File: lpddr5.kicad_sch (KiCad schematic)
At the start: 38 parts, among them U1 MT62F1G32D4DR-031_WT:B

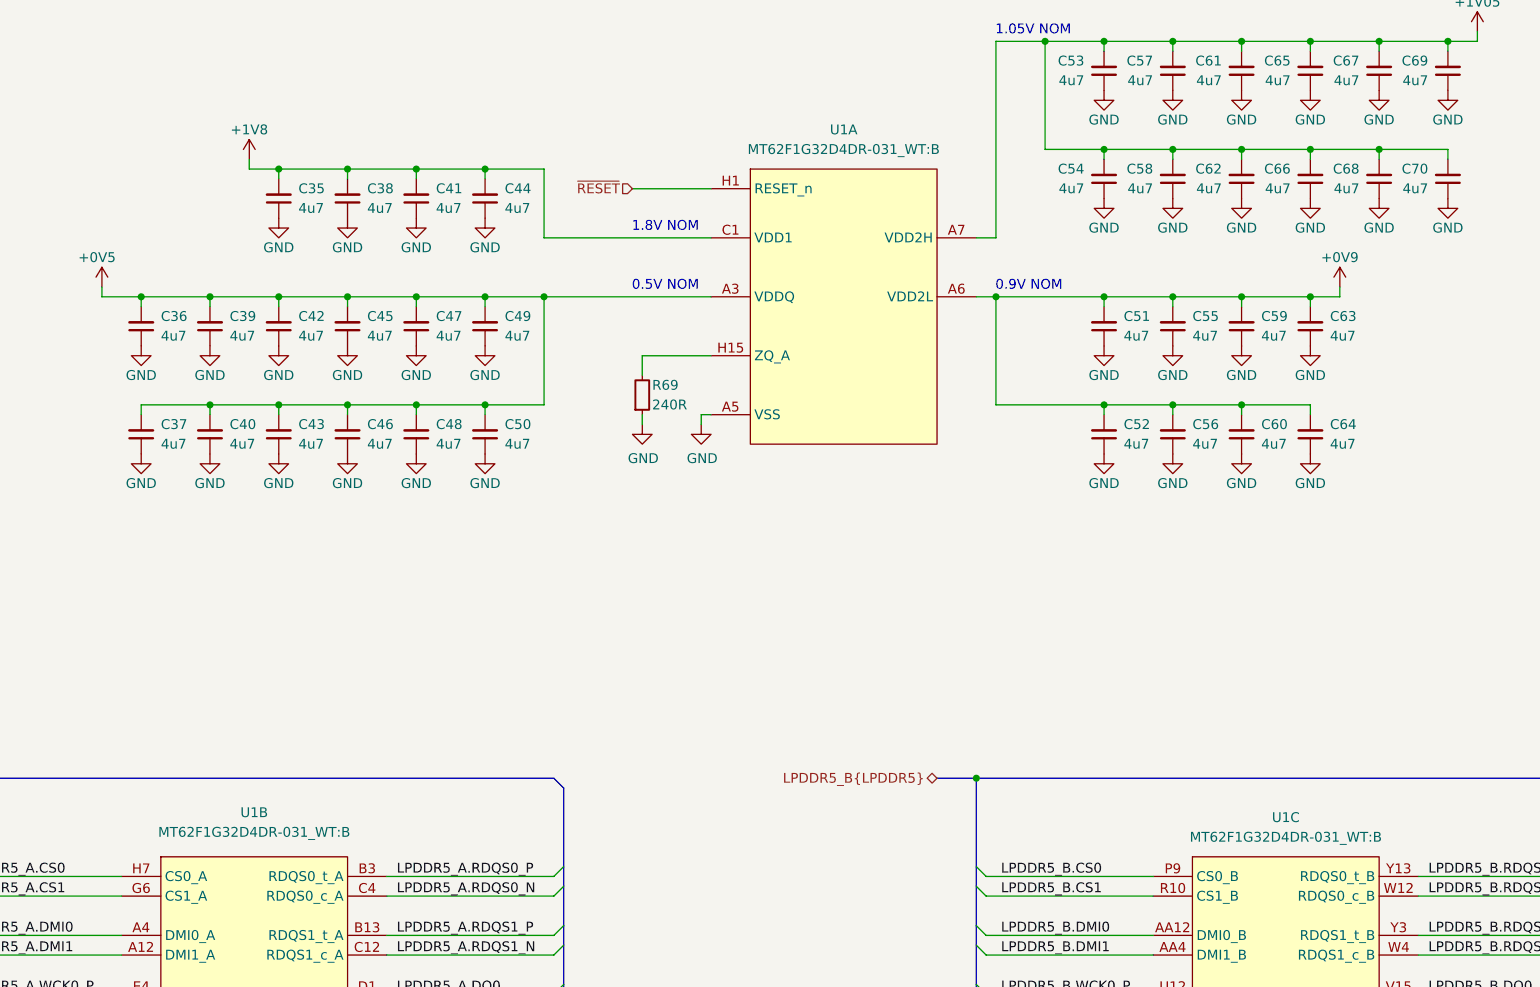
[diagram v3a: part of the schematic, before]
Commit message: [#52835] schematics: update components after standardization
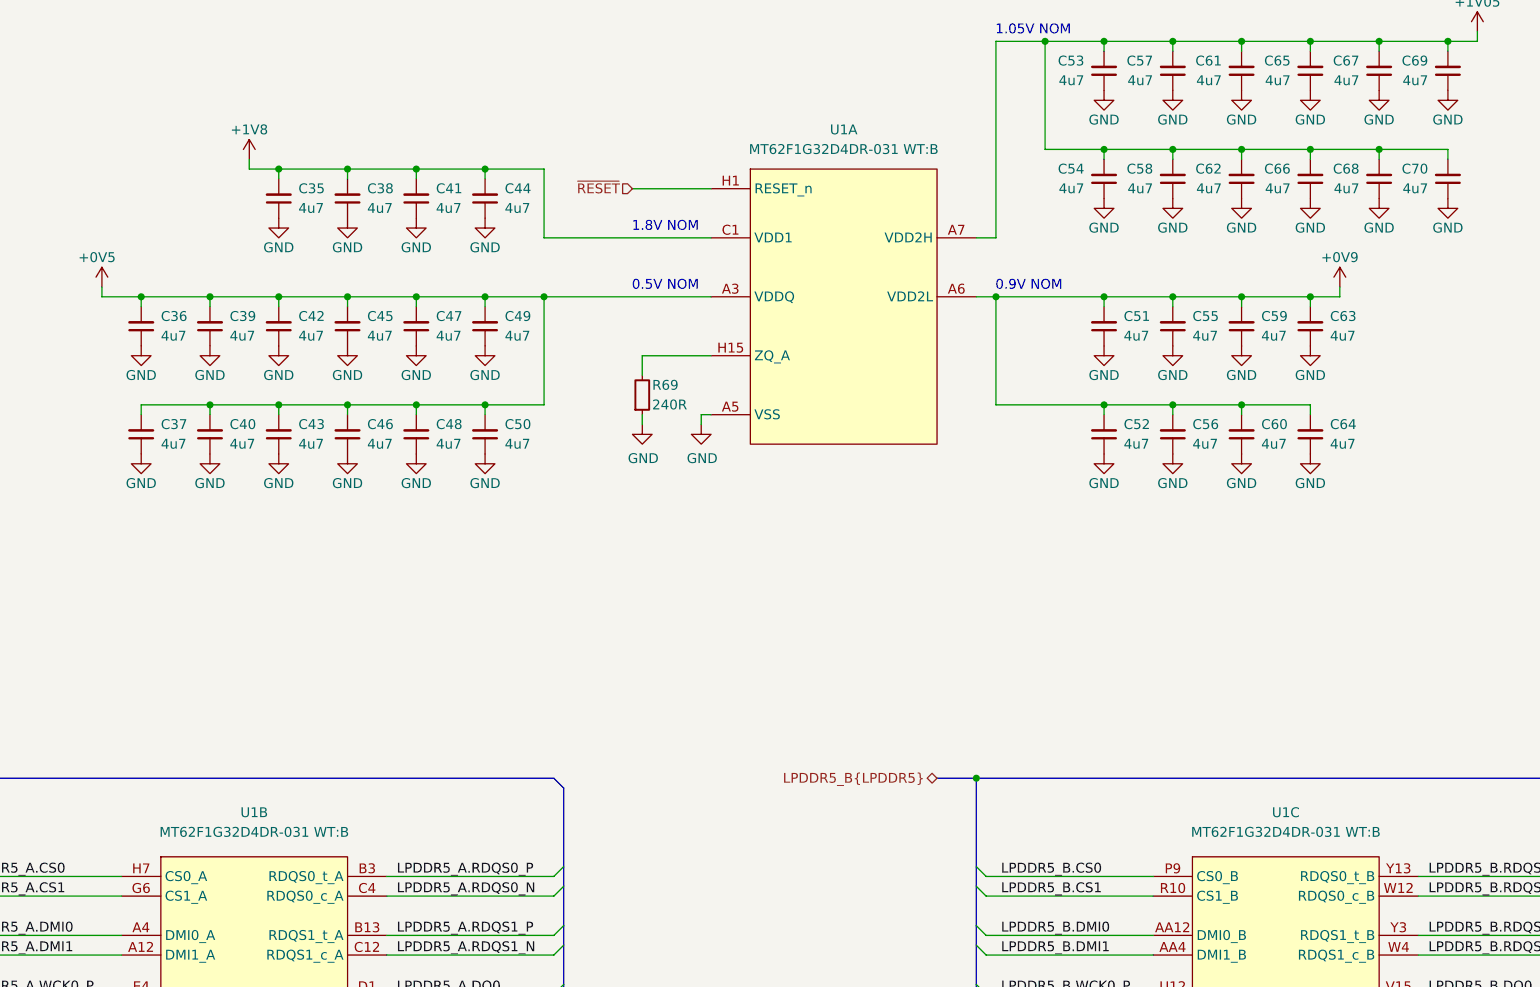
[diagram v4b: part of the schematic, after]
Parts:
- removed U1: MT62F1G32D4DR-031_WT:B, antmicro-footprints:BGA-315_12.4x15mm_Layout15x21_P0.7x0.8mm, symbol antmicroMemory:MT62F1G32D4DR-031_WT{colon}B
- added U1: MT62F1G32D4DR-031, antmicro-footprints:BGA-315_12.4x15mm_Layout15x21_P0.8x0.7mm, symbol antmicroMemory:MT62F1G32D4DR-031
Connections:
- net +0V5: now also U1.A13 (VDDQ), U1.A3 (VDDQ), U1.AA13 (VDDQ), U1.AA3 (VDDQ), U1.B14 (VDDQ), U1.B2 (VDDQ), U1.C13 (VDDQ), U1.C3 (VDDQ), U1.D12 (VDDQ), U1.D4 (VDDQ), U1.E11 (VDDQ), U1.E5 (VDDQ), U1.F1 (VDDQ), U1.F12 (VDDQ), U1.F13 (VDDQ), U1.F15 (VDDQ), U1.F3 (VDDQ), U1.F4 (VDDQ), U1.G1 (VDDQ), U1.G14 (VDDQ), U1.G15 (VDDQ), U1.G2 (VDDQ), U1.R1 (VDDQ), U1.R14 (VDDQ), U1.R15 (VDDQ), U1.R2 (VDDQ), U1.T1 (VDDQ), U1.T12 (VDDQ), U1.T13 (VDDQ), U1.T15 (VDDQ), U1.T3 (VDDQ), U1.T4 (VDDQ), U1.U11 (VDDQ), U1.U5 (VDDQ), U1.V12 (VDDQ), U1.V4 (VDDQ), U1.W13 (VDDQ), U1.W3 (VDDQ), U1.Y14 (VDDQ), U1.Y2 (VDDQ)
- net +0V9: now also U1.A10 (VDD2L), U1.A6 (VDD2L), U1.AA10 (VDD2L), U1.AA6 (VDD2L), U1.B10 (VDD2L), U1.B6 (VDD2L), U1.H14 (VDD2L), U1.H2 (VDD2L), U1.J14 (VDD2L), U1.J2 (VDD2L), U1.N14 (VDD2L), U1.N2 (VDD2L), U1.P14 (VDD2L), U1.P2 (VDD2L), U1.Y10 (VDD2L), U1.Y6 (VDD2L)
- net +1V05: now also U1.A7 (VDD2H), U1.A8 (VDD2H), U1.A9 (VDD2H), U1.AA7 (VDD2H), U1.AA8 (VDD2H), U1.AA9 (VDD2H), U1.B7 (VDD2H), U1.B9 (VDD2H), U1.C7 (VDD2H), U1.C9 (VDD2H), U1.D8 (VDD2H), U1.E7 (VDD2H), U1.E9 (VDD2H), U1.F10 (VDD2H), U1.F6 (VDD2H), U1.F7 (VDD2H), U1.F9 (VDD2H), U1.J11 (VDD2H), U1.J5 (VDD2H), U1.K1 (VDD2H), U1.K10 (VDD2H), U1.K11 (VDD2H), U1.K12 (VDD2H), U1.K13 (VDD2H), U1.K14 (VDD2H), U1.K15 (VDD2H), U1.K2 (VDD2H), U1.K3 (VDD2H), U1.K4 (VDD2H), U1.K5 (VDD2H), U1.K6 (VDD2H), U1.L10 (VDD2H), U1.L6 (VDD2H), U1.L7 (VDD2H), U1.L8 (VDD2H), U1.L9 (VDD2H), U1.M1 (VDD2H), U1.M10 (VDD2H), U1.M11 (VDD2H), U1.M12 (VDD2H), U1.M13 (VDD2H), U1.M14 (VDD2H), U1.M15 (VDD2H), U1.M2 (VDD2H), U1.M3 (VDD2H), U1.M4 (VDD2H), U1.M5 (VDD2H), U1.M6 (VDD2H), U1.N11 (VDD2H), U1.N5 (VDD2H), U1.T10 (VDD2H), U1.T6 (VDD2H), U1.T7 (VDD2H), U1.T9 (VDD2H), U1.U7 (VDD2H), U1.U9 (VDD2H), U1.V8 (VDD2H), U1.W7 (VDD2H), U1.W9 (VDD2H), U1.Y7 (VDD2H), U1.Y9 (VDD2H)
- net +1V8: now also U1.C1 (VDD1), U1.C15 (VDD1), U1.W1 (VDD1), U1.W15 (VDD1)
- net GND: now also U1.A11 (VSS), U1.A5 (VSS), U1.AA11 (VSS), U1.AA5 (VSS), U1.B12 (VSS), U1.B4 (VSS), U1.B8 (VSS), U1.C11 (VSS), U1.C5 (VSS), U1.C8 (VSS), U1.D10 (VSS), U1.D14 (VSS), U1.D2 (VSS), U1.D6 (VSS), U1.D7 (VSS), U1.D9 (VSS), U1.E1 (VSS), U1.E13 (VSS), U1.E15 (VSS), U1.E3 (VSS), U1.E8 (VSS), U1.F14 (VSS), U1.F2 (VSS), U1.F8 (VSS), U1.G11 (VSS), U1.G13 (VSS), U1.G3 (VSS), U1.G5 (VSS), U1.G7 (VSS), U1.G9 (VSS), U1.H10 (VSS), U1.H12 (VSS), U1.H3 (VSS), U1.H4 (VSS), U1.H6 (VSS), U1.H8 (VSS), U1.J1 (VSS), U1.J10 (VSS), U1.J12 (VSS), U1.J13 (VSS), U1.J15 (VSS), U1.J3 (VSS), U1.J7 (VSS), U1.J8 (VSS), U1.K7 (VSS), U1.K8 (VSS), U1.K9 (VSS), U1.L1 (VSS), U1.L11 (VSS), U1.L12 (VSS), U1.L13 (VSS), U1.L14 (VSS), U1.L15 (VSS), U1.L2 (VSS), U1.L3 (VSS), U1.L4 (VSS), U1.L5 (VSS), U1.M7 (VSS), U1.M8 (VSS), U1.M9 (VSS), U1.N1 (VSS), U1.N10 (VSS), U1.N12 (VSS), U1.N13 (VSS), U1.N15 (VSS), U1.N3 (VSS), U1.N4 (VSS), U1.N6 (VSS), U1.N8 (VSS), U1.N9 (VSS), U1.P10 (VSS), U1.P12 (VSS), U1.P13 (VSS), U1.P4 (VSS), U1.P6 (VSS), U1.P8 (VSS), U1.R11 (VSS), U1.R13 (VSS), U1.R3 (VSS), U1.R5 (VSS), U1.R7 (VSS), U1.R9 (VSS), U1.T14 (VSS), U1.T2 (VSS), U1.T8 (VSS), U1.U1 (VSS), U1.U13 (VSS), U1.U15 (VSS), U1.U3 (VSS), U1.U8 (VSS), U1.V10 (VSS), U1.V14 (VSS), U1.V2 (VSS), U1.V6 (VSS), U1.V7 (VSS), U1.V9 (VSS), U1.W11 (VSS), U1.W5 (VSS), U1.W8 (VSS), U1.Y12 (VSS), U1.Y4 (VSS), U1.Y8 (VSS)
- net LPDDR5_A.CA0: now also U1.G4 (CA0_A)
- net LPDDR5_A.CA1: now also U1.H5 (CA1_A)
- net LPDDR5_A.CA2: now also U1.G8 (CA2_A)
- net LPDDR5_A.CA3: now also U1.H11 (CA3_A)
- net LPDDR5_A.CA4: now also U1.G10 (CA4_A)
- net LPDDR5_A.CA5: now also U1.H13 (CA5_A)
- net LPDDR5_A.CA6: now also U1.G12 (CA6_A)
- net LPDDR5_A.CK_N: now also U1.J9 (CK_c_A)
- net LPDDR5_A.CK_P: now also U1.H9 (CK_t_A)
- net LPDDR5_A.CS0: now also U1.H7 (CS0_A)
- net LPDDR5_A.CS1: now also U1.G6 (CS1_A)
- net LPDDR5_A.DMI0: now also U1.A4 (DMI0_A)
- net LPDDR5_A.DMI1: now also U1.A12 (DMI1_A)
- net LPDDR5_A.DQ0: now also U1.D1 (DQ0_A)
- net LPDDR5_A.DQ1: now also U1.C2 (DQ1_A)
- net LPDDR5_A.DQ10: now also U1.E14 (DQ10_A)
- net LPDDR5_A.DQ11: now also U1.D13 (DQ11_A)
- net LPDDR5_A.DQ12: now also U1.B11 (DQ12_A)
- net LPDDR5_A.DQ13: now also U1.C10 (DQ13_A)
- net LPDDR5_A.DQ14: now also U1.E10 (DQ14_A)
- net LPDDR5_A.DQ15: now also U1.F11 (DQ15_A)
- net LPDDR5_A.DQ2: now also U1.E2 (DQ2_A)
- net LPDDR5_A.DQ3: now also U1.D3 (DQ3_A)
- net LPDDR5_A.DQ4: now also U1.B5 (DQ4_A)
- net LPDDR5_A.DQ5: now also U1.C6 (DQ5_A)
- net LPDDR5_A.DQ6: now also U1.E6 (DQ6_A)
- net LPDDR5_A.DQ7: now also U1.F5 (DQ7_A)
- net LPDDR5_A.DQ8: now also U1.D15 (DQ8_A)
- net LPDDR5_A.DQ9: now also U1.C14 (DQ9_A)
- net LPDDR5_A.RDQS0_N: now also U1.C4 (RDQS0_c_A)
- net LPDDR5_A.RDQS0_P: now also U1.B3 (RDQS0_t_A)
- net LPDDR5_A.RDQS1_N: now also U1.C12 (RDQS1_c_A)
- net LPDDR5_A.RDQS1_P: now also U1.B13 (RDQS1_t_A)
- net LPDDR5_A.WCK0_N: now also U1.D5 (WCK0_c_A)
- net LPDDR5_A.WCK0_P: now also U1.E4 (WCK0_t_A)
- net LPDDR5_A.WCK1_N: now also U1.D11 (WCK1_c_A)
- net LPDDR5_A.WCK1_P: now also U1.E12 (WCK1_t_A)
- net LPDDR5_B.CA0: now also U1.R12 (CA0_B)
- net LPDDR5_B.CA1: now also U1.P11 (CA1_B)
- net LPDDR5_B.CA2: now also U1.R8 (CA2_B)
- net LPDDR5_B.CA3: now also U1.P5 (CA3_B)
- net LPDDR5_B.CA4: now also U1.R6 (CA4_B)
- net LPDDR5_B.CA5: now also U1.P3 (CA5_B)
- net LPDDR5_B.CA6: now also U1.R4 (CA6_B)
- net LPDDR5_B.CK_N: now also U1.N7 (CK_c_B)
- net LPDDR5_B.CK_P: now also U1.P7 (CK_t_B)
- net LPDDR5_B.CS0: now also U1.P9 (CS0_B)
- net LPDDR5_B.CS1: now also U1.R10 (CS1_B)
- net LPDDR5_B.DMI0: now also U1.AA12 (DMI0_B)
- net LPDDR5_B.DMI1: now also U1.AA4 (DMI1_B)
- net LPDDR5_B.DQ0: now also U1.V15 (DQ0_B)
- net LPDDR5_B.DQ1: now also U1.W14 (DQ1_B)
- net LPDDR5_B.DQ10: now also U1.U2 (DQ10_B)
- net LPDDR5_B.DQ11: now also U1.V3 (DQ11_B)
- net LPDDR5_B.DQ12: now also U1.Y5 (DQ12_B)
- net LPDDR5_B.DQ13: now also U1.W6 (DQ13_B)
- net LPDDR5_B.DQ14: now also U1.U6 (DQ14_B)
- net LPDDR5_B.DQ15: now also U1.T5 (DQ15_B)
- net LPDDR5_B.DQ2: now also U1.U14 (DQ2_B)
- net LPDDR5_B.DQ3: now also U1.V13 (DQ3_B)
- net LPDDR5_B.DQ4: now also U1.Y11 (DQ4_B)
- net LPDDR5_B.DQ5: now also U1.W10 (DQ5_B)
- net LPDDR5_B.DQ6: now also U1.U10 (DQ6_B)
- net LPDDR5_B.DQ7: now also U1.T11 (DQ7_B)
- net LPDDR5_B.DQ8: now also U1.V1 (DQ8_B)
- net LPDDR5_B.DQ9: now also U1.W2 (DQ9_B)
- net LPDDR5_B.RDQS0_N: now also U1.W12 (RDQS0_c_B)
- net LPDDR5_B.RDQS0_P: now also U1.Y13 (RDQS0_t_B)
- net LPDDR5_B.RDQS1_N: now also U1.W4 (RDQS1_c_B)
- net LPDDR5_B.RDQS1_P: now also U1.Y3 (RDQS1_t_B)
- net LPDDR5_B.WCK0_N: now also U1.V11 (WCK0_c_B)
- net LPDDR5_B.WCK0_P: now also U1.U12 (WCK0_t_B)
- net LPDDR5_B.WCK1_N: now also U1.V5 (WCK1_c_B)
- net LPDDR5_B.WCK1_P: now also U1.U4 (WCK1_t_B)
- net ~{RESET}: now also U1.H1 (RESET_n)
- net at R69.2: now also U1.H15 (ZQ_A)

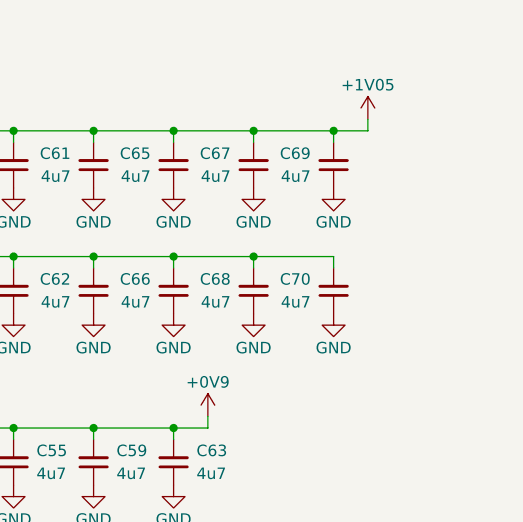
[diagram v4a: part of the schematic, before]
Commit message: [#52536] schematics: add additional decoupling to DDR die
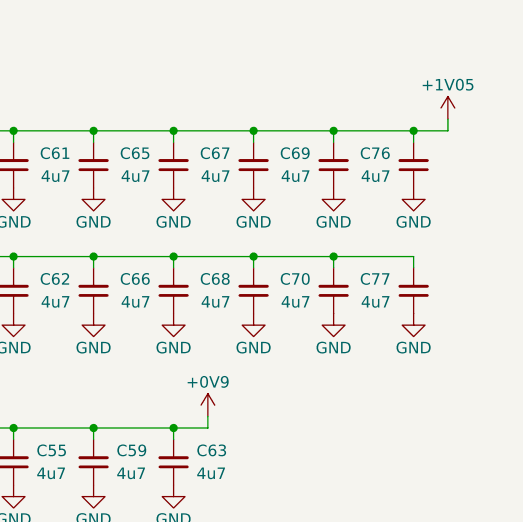
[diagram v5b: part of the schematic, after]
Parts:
- added C76, C77: C_4u7_0402, antmicro-footprints:C_0402_1005Metric, symbol antmicroCapacitors0402:C_4u7_0402
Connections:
- net +1V05: now also C76.2, C77.2
- net GND: now also C76.1, C77.1
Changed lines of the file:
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@@
   (junction (at 80.01 129.54) (diameter 0) (color 0 0 0 0)
   )
+  (junction (at 283.21 34.29) (diameter 0) (color 0 0 0 0)
+  )
   (junction (at 229.87 81.28) (diameter 0) (color 0 0 0 0)
   )
@@
   (junction (at 140.97 50.8) (diameter 0) (color 0 0 0 0)
   )
+  (junction (at 274.32 34.29) (diameter 0) (color 0 0 0 0)
+  )
   (junction (at 114.3 81.28) (diameter 0) (color 0 0 0 0)
   )
@@
   (junction (at 149.86 50.8) (diameter 0) (color 0 0 0 0)
   )
-  (junction (at 256.54 34.29) (diameter 0) (color 0 0 0 0)
+  (junction (at 274.32 48.26) (diameter 0) (color 0 0 0 0)
   )
-  (junction (at 274.32 34.29) (diameter 0) (color 0 0 0 0)
+  (junction (at 256.54 34.29) (diameter 0) (color 0 0 0 0)
   )
   (bus_entry (at 160.02 191.77) (size -1.27 1.27)
@@
     (stroke (width 0) (type default) (color 0 0 0 0))
   )
+  (wire (pts (xy 283.21 34.29) (xy 283.21 35.56))
+    (stroke (width 0) (type default) (color 0 0 0 0))
+  )
   (wire (pts (xy 247.65 48.26) (xy 247.65 49.53))
     (stroke (width 0) (type default) (color 0 0 0 0))
@@
     (stroke (width 0) (type default) (color 0 0 0 0))
   )
+  (wire (pts (xy 274.32 34.29) (xy 283.21 34.29))
+    (stroke (width 0) (type default) (color 0 0 0 0))
+  )
   (bus (pts (xy 293.37 130.81) (xy 293.37 140.97))
     (stroke (width 0) (type default) (color 0 0 0 0))
@@
     (stroke (width 0) (type default) (color 0 0 0 0))
   )
+  (wire (pts (xy 265.43 34.29) (xy 274.32 34.29))
+    (stroke (width 0) (type default) (color 0 0 0 0))
+  )
   (bus (pts (xy 213.36 189.23) (xy 213.36 191.77))
     (stroke (width 0) (type default) (color 0 0 0 0))
@@
     (stroke (width 0) (type default) (color 0 0 0 0))
   )
+  (wire (pts (xy 287.02 33.02) (xy 287.02 34.29))
+    (stroke (width 0) (type default) (color 0 0 0 0))
+  )
   (wire (pts (xy 215.9 59.69) (xy 213.36 59.69))
     (stroke (width 0) (type default) (color 0 0 0 0))
@@
     (stroke (width 0) (type default) (color 0 0 0 0))
   )
-  (wire (pts (xy 278.13 34.29) (xy 274.32 34.29))
-    (stroke (width 0) (type default) (color 0 0 0 0))
-  )
   (wire (pts (xy 214.63 187.96) (xy 236.22 187.96))
     (stroke (width 0) (type default) (color 0 0 0 0))
@@
     (stroke (width 0) (type default) (color 0 0 0 0))
   )
+  (wire (pts (xy 283.21 48.26) (xy 274.32 48.26))
+    (stroke (width 0) (type default) (color 0 0 0 0))
+  )
   (wire (pts (xy 137.16 162.56) (xy 158.75 162.56))
     (stroke (width 0) (type default) (color 0 0 0 0))
@@
     (stroke (width 0) (type default) (color 0 0 0 0))
   )
+  (wire (pts (xy 283.21 48.26) (xy 283.21 49.53))
+    (stroke (width 0) (type default) (color 0 0 0 0))
+  )
   (wire (pts (xy 214.63 165.1) (xy 236.22 165.1))
     (stroke (width 0) (type default) (color 0 0 0 0))
@@
     (stroke (width 0) (type default) (color 0 0 0 0))
   )
-  (wire (pts (xy 278.13 33.02) (xy 278.13 34.29))
-    (stroke (width 0) (type default) (color 0 0 0 0))
-  )
   (wire (pts (xy 81.28 185.42) (xy 102.87 185.42))
     (stroke (width 0) (type default) (color 0 0 0 0))
   )
-  (wire (pts (xy 265.43 34.29) (xy 274.32 34.29))
+  (wire (pts (xy 287.02 34.29) (xy 283.21 34.29))
     (stroke (width 0) (type default) (color 0 0 0 0))
   )
@@
     (pin "1")
   )
+  (symbol (lib_id "antmicropower:+1V05") (at 287.02 33.02 0) (unit 1)
+    (in_bom yes) (on_board yes)
+    (property "Reference" "#PWR0146" (id 0) (at 287.02 36.83 0)
+      (effects (font (size 1.27 1.27)) hide)
+    )
+    (property "Value" "+1V05" (id 1) (at 287.02 29.21 0))
+    (property "Footprint" "" (id 2) (at 287.02 33.02 0)
+      (effects (font (size 1.27 1.27)) hide)
+    )
+    (property "Datasheet" "" (id 3) (at 287.02 33.02 0)
+      (effects (font (size 1.27 1.27)) hide)
+    )
+    (pin "1")
+  )
   (symbol (lib_id "lpddr5-sodimm:GND") (at 140.97 87.63 0) (unit 1)
     (in_bom yes) (on_board yes)
@@
     (pin "1")
   )
+  (symbol (lib_id "antmicroCapacitors0402:C_4u7_0402") (at 283.21 54.61 270) (mirror x) (unit 1)
+    (in_bom yes) (on_board yes) (fields_autoplaced)
+    (property "Reference" "C77" (id 0) (at 280.67 50.7935 90)
+      (effects (font (size 1.27 1.27) (thickness 0.15)) (justify right))
+    )
+    (property "Value" "C_4u7_0402" (id 1) (at 273.05 34.29 0)
+      (effects (font (size 1.27 1.27) (thickness 0.15)) (justify left bottom) hide)
+    )
+    (property "Footprint" "antmicro-footprints:C_0402_1005Metric" (id 2) (at 270.51 34.29 0)
+      (effects (font (size 1.27 1.27) (thickness 0.15)) (justify left bottom) hide)
+    )
+    (property "Datasheet" "https://www.murata.com/products/productdetail?partno=GRM155R61A475MEAA%23" (id 3) (at 267.97 34.29 0)
+      (effects (font (size 1.27 1.27) (thickness 0.15)) (justify left bottom) hide)
+    )
+    (property "MPN" "GRM155R61A475MEAAD" (id 4) (at 265.43 34.29 0)
+      (effects (font (size 1.27 1.27) (thickness 0.15)) (justify left bottom) hide)
+    )
+    (property "Manufacturer" "Murata" (id 5) (at 262.89 34.29 0)
+      (effects (font (size 1.27 1.27) (thickness 0.15)) (justify left bottom) hide)
+    )
+    (property "License" "Apache-2.0" (id 6) (at 260.35 34.29 0)
+      (effects (font (size 1.27 1.27) (thickness 0.15)) (justify left bottom) hide)
+    )
+    (property "Author" "Antmicro" (id 7) (at 257.81 34.29 0)
+      (effects (font (size 1.27 1.27) (thickness 0.15)) (justify left bottom) hide)
+    )
+    (property "Val" "4u7" (id 8) (at 280.67 53.3335 90)
+      (effects (font (size 1.27 1.27) (thickness 0.15)) (justify right))
+    )
+    (property "Voltage" "" (id 9) (at 255.27 34.29 0)
+      (effects (font (size 1.27 1.27)) (justify left bottom) hide)
+    )
+    (property "Dielectric" "" (id 10) (at 252.73 34.29 0)
+      (effects (font (size 1.27 1.27)) (justify left bottom) hide)
+    )
+    (pin "1")
+    (pin "2")
+  )
   (symbol (lib_id "lpddr5-sodimm:GND") (at 140.97 73.66 0) (unit 1)
     (in_bom yes) (on_board yes)
@@
     (pin "2")
   )
-  (symbol (lib_id "antmicropower:+1V05") (at 278.13 33.02 0) (unit 1)
-    (in_bom yes) (on_board yes)
-    (property "Reference" "#PWR0146" (id 0) (at 278.13 36.83 0)
-      (effects (font (size 1.27 1.27)) hide)
-    )
-    (property "Value" "+1V05" (id 1) (at 278.13 29.21 0))
-    (property "Footprint" "" (id 2) (at 278.13 33.02 0)
-      (effects (font (size 1.27 1.27)) hide)
-    )
-    (property "Datasheet" "" (id 3) (at 278.13 33.02 0)
-      (effects (font (size 1.27 1.27)) hide)
-    )
-    (pin "1")
-  )
   (symbol (lib_id "antmicropower:+0V5") (at 100.33 66.04 0) (unit 1)
     (in_bom yes) (on_board yes)
@@
     (pin "1")
   )
+  (symbol (lib_id "lpddr5-sodimm:GND") (at 283.21 54.61 0) (mirror y) (unit 1)
+    (in_bom yes) (on_board yes)
+    (property "Reference" "#PWR0271" (id 0) (at 283.21 60.96 0)
+      (effects (font (size 1.27 1.27)) hide)
+    )
+    (property "Value" "GND" (id 1) (at 283.21 58.42 0))
+    (property "Footprint" "" (id 2) (at 283.21 54.61 0)
+      (effects (font (size 1.27 1.27)) hide)
+    )
+    (property "Datasheet" "" (id 3) (at 283.21 54.61 0)
+      (effects (font (size 1.27 1.27)) hide)
+    )
+    (pin "1")
+  )
   (symbol (lib_id "antmicropower:+1V8") (at 119.38 49.53 0) (unit 1)
     (in_bom yes) (on_board yes)
@@
     (pin "1")
   )
+  (symbol (lib_id "lpddr5-sodimm:GND") (at 283.21 40.64 0) (mirror y) (unit 1)
+    (in_bom yes) (on_board yes)
+    (property "Reference" "#PWR0225" (id 0) (at 283.21 46.99 0)
+      (effects (font (size 1.27 1.27)) hide)
+    )
+    (property "Value" "GND" (id 1) (at 283.21 44.45 0))
+    (property "Footprint" "" (id 2) (at 283.21 40.64 0)
+      (effects (font (size 1.27 1.27)) hide)
+    )
+    (property "Datasheet" "" (id 3) (at 283.21 40.64 0)
+      (effects (font (size 1.27 1.27)) hide)
+    )
+    (pin "1")
+  )
+  (symbol (lib_id "antmicroCapacitors0402:C_4u7_0402") (at 283.21 40.64 270) (mirror x) (unit 1)
+    (in_bom yes) (on_board yes) (fields_autoplaced)
+    (property "Reference" "C76" (id 0) (at 280.67 36.8235 90)
+      (effects (font (size 1.27 1.27) (thickness 0.15)) (justify right))
+    )
+    (property "Value" "C_4u7_0402" (id 1) (at 273.05 20.32 0)
+      (effects (font (size 1.27 1.27) (thickness 0.15)) (justify left bottom) hide)
+    )
+    (property "Footprint" "antmicro-footprints:C_0402_1005Metric" (id 2) (at 270.51 20.32 0)
+      (effects (font (size 1.27 1.27) (thickness 0.15)) (justify left bottom) hide)
+    )
+    (property "Datasheet" "https://www.murata.com/products/productdetail?partno=GRM155R61A475MEAA%23" (id 3) (at 267.97 20.32 0)
+      (effects (font (size 1.27 1.27) (thickness 0.15)) (justify left bottom) hide)
+    )
+    (property "MPN" "GRM155R61A475MEAAD" (id 4) (at 265.43 20.32 0)
+      (effects (font (size 1.27 1.27) (thickness 0.15)) (justify left bottom) hide)
+    )
+    (property "Manufacturer" "Murata" (id 5) (at 262.89 20.32 0)
+      (effects (font (size 1.27 1.27) (thickness 0.15)) (justify left bottom) hide)
+    )
+    (property "License" "Apache-2.0" (id 6) (at 260.35 20.32 0)
+      (effects (font (size 1.27 1.27) (thickness 0.15)) (justify left bottom) hide)
+    )
+    (property "Author" "Antmicro" (id 7) (at 257.81 20.32 0)
+      (effects (font (size 1.27 1.27) (thickness 0.15)) (justify left bottom) hide)
+    )
+    (property "Val" "4u7" (id 8) (at 280.67 39.3635 90)
+      (effects (font (size 1.27 1.27) (thickness 0.15)) (justify right))
+    )
+    (property "Voltage" "" (id 9) (at 255.27 20.32 0)
+      (effects (font (size 1.27 1.27)) (justify left bottom) hide)
+    )
+    (property "Dielectric" "" (id 10) (at 252.73 20.32 0)
+      (effects (font (size 1.27 1.27)) (justify left bottom) hide)
+    )
+    (pin "1")
+    (pin "2")
+  )
   (symbol (lib_id "lpddr5-sodimm:GND") (at 229.87 40.64 0) (mirror y) (unit 1)

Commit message: [#52835] update project name
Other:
- title: LPDDR5 SO-DIMM -> LPDDR5 Testbed

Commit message: Loclib
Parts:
- C35, C36, C37, C38, C39, C40, C41, C42, C43, C44, C45, C46, C47, C48, C49, C50, C51, C52, C53, C54, C55, C56, C57, C58, C59, C60, C61, C62, C63, C64, C65, C66, C67, C68, C69, C70, C76, C77: footprint antmicro-footprints:C_0402_1005Metric -> lpddr5-testbed-footprints:C_0402_1005Metric; symbol antmicroCapacitors0402:C_4u7_0402 -> lpddr5-testbed:C_4u7_0402
- R69: footprint antmicro-footprints:R_0402_1005Metric -> lpddr5-testbed-footprints:R_0402_1005Metric; symbol antmicroResistors0402:R_240R_0402 -> lpddr5-testbed:R_240R_0402
- U1: footprint antmicro-footprints:BGA-315_12.4x15mm_Layout15x21_P0.8x0.7mm -> lpddr5-testbed-footprints:BGA-315_12.4x15mm_Layout15x21_P0.8x0.7mm; symbol antmicroMemory:MT62F1G32D4DR-031 -> lpddr5-testbed:MT62F1G32D4DR-031
